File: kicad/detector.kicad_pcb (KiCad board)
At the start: 4 copper layers, 38.5 x 35.8 mm, 45 parts, among them J1 Conn_01x05_Male, J2 Conn_01x05_Male, M2.5 MountingHole_2.7mm_M2.5_ISO73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, U1 LT1761-5, U2 LT1964-5, U3 REF5010ID, U4 OPA2197xD, U5 OPA2197xD

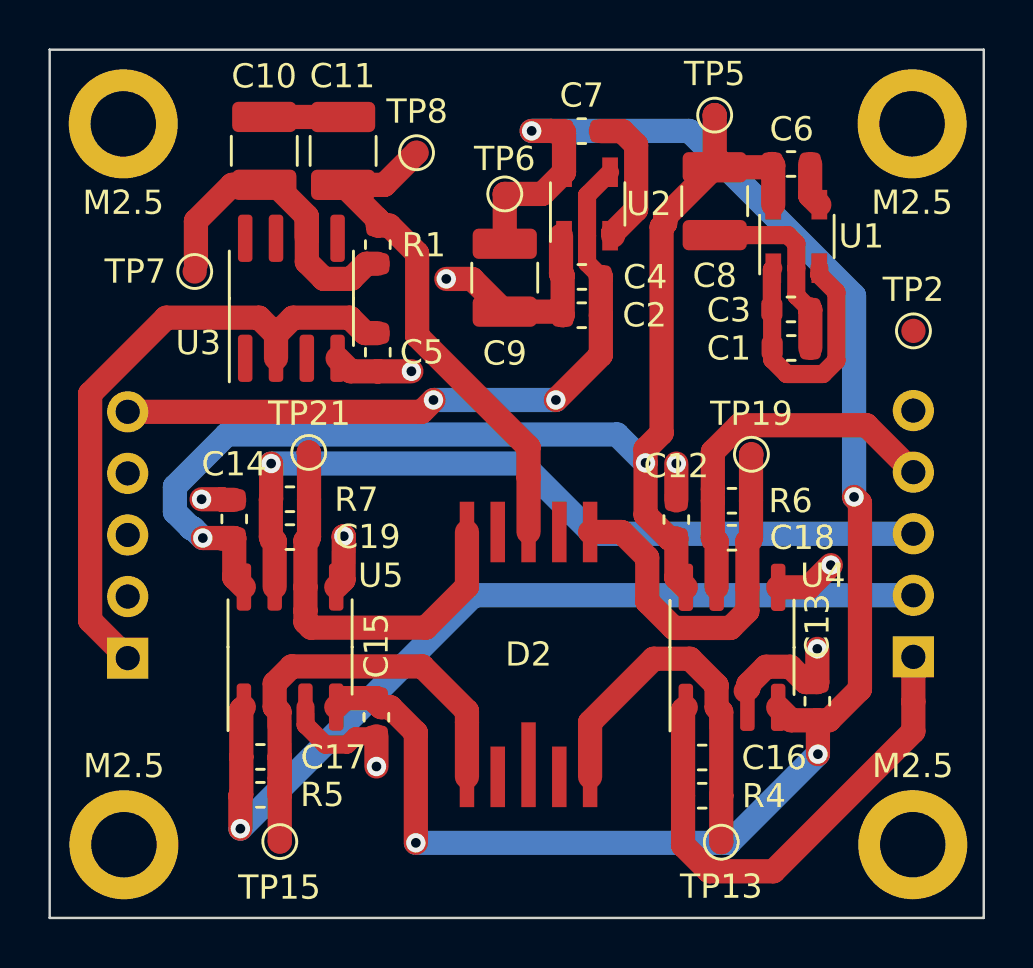
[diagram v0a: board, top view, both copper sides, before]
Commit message: applied ground-poor, via-stitching, added logo and rev to boards
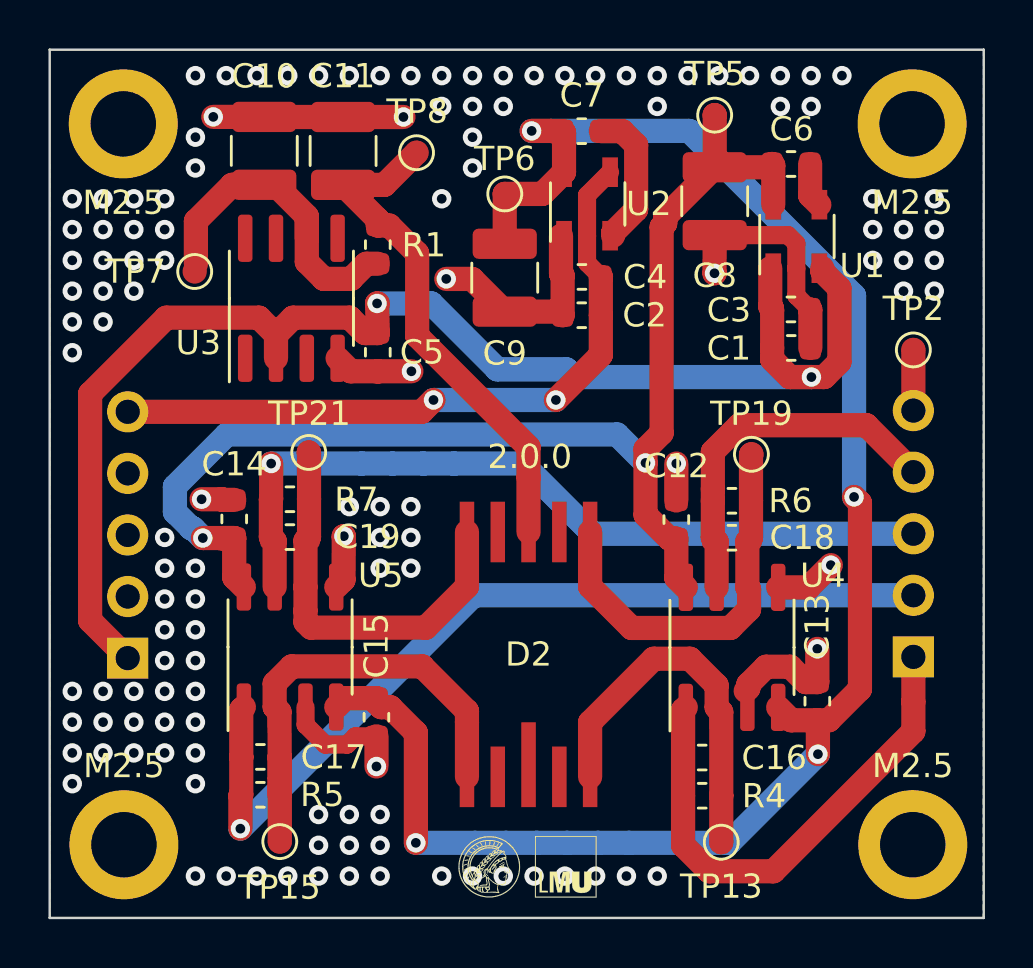
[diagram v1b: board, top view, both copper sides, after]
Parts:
- added G***: LOGO, Common:mpq_lmu_logo, F.Cu at (164.9, 148.2)
- moved TP2 0.79 mm to (180.7, 126.9)
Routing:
- net +12V: track 37.6 -> 58.3 mm, vias 0 -> 2
- net GND: track 41.5 -> 50.2 mm, vias 8 -> 124
- net (no net): vias 0 -> 2
- added copper zone on B.Cu, net GND
- added copper zone on F.Cu, net GND
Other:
- board text added: "2.0.0"

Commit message: disabled fill zones, removed vias
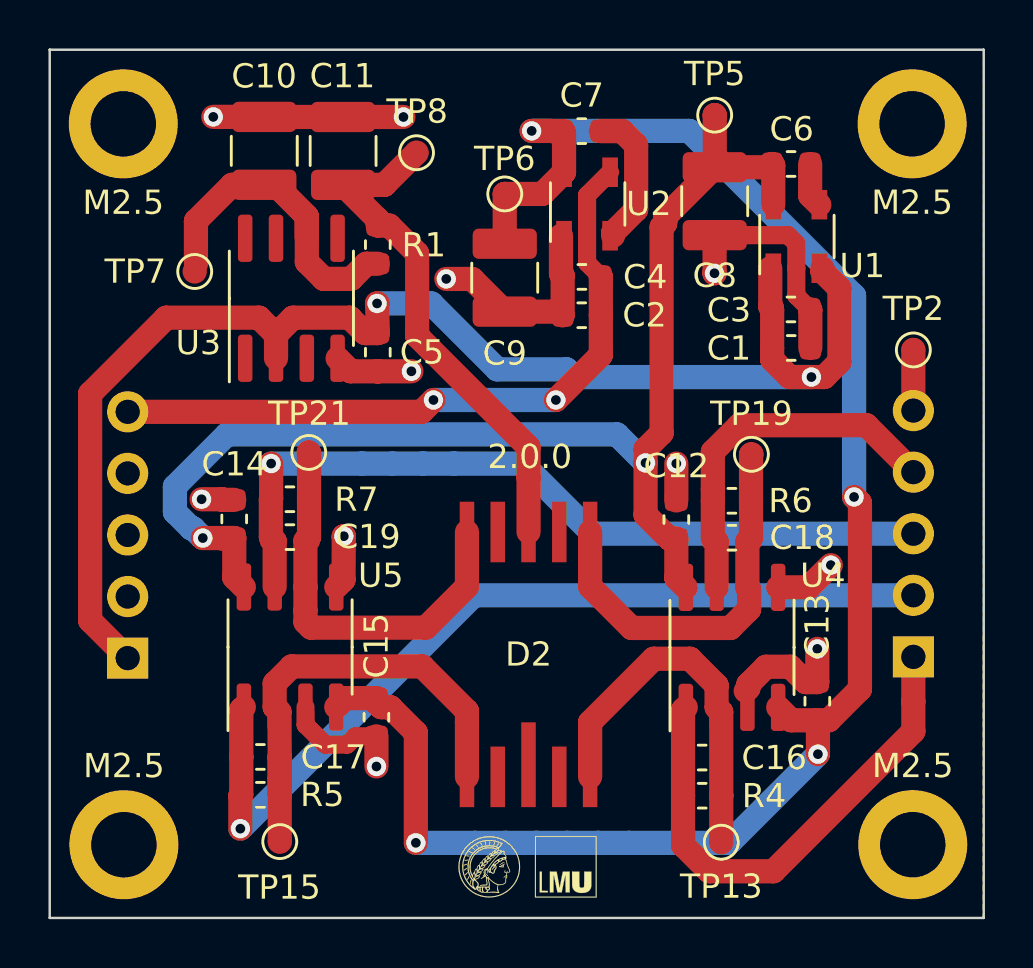
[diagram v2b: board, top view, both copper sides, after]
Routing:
- net GND: vias 124 -> 11
- net (no net): vias 2 -> 0
